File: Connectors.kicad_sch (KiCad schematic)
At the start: 4 parts, among them J1 Conn_01x09_Pin, J2 Conn_02x03_Odd_Even

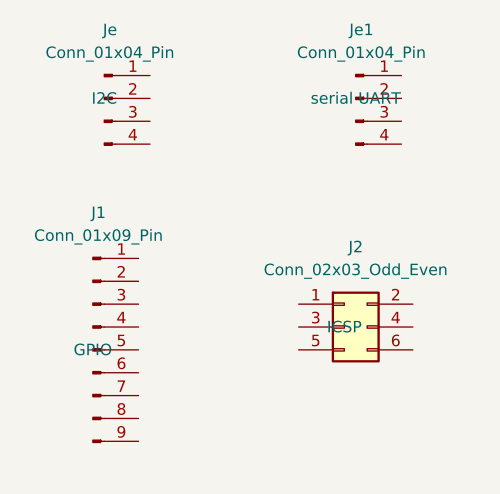
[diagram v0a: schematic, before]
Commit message: Changed location of symbols (arrange).
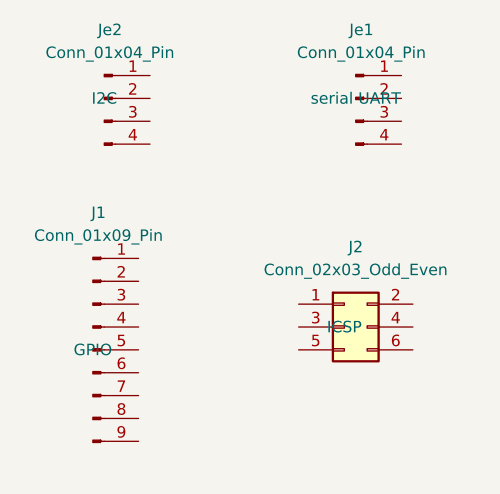
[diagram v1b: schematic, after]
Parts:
- renumbered Je to Je2
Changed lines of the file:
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@@
 		(dnp no)
 		(fields_autoplaced yes)
-		(property "Reference" "Je"
+		(property "Reference" "Je2"
 			(at 121.285 81.28 0)
 			(effects
@@
 			(project ""
 				(path "/b34ba724-37f1-4069-92d1-dfc9c20970e0/121f44e2-27fc-4ef2-96b3-bc3990488b1d"
-					(reference "Je")
+					(reference "Je2")
 					(unit 1)
 				)

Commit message: completed symbol-footprint assiciations
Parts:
- J1: footprint (none) -> Connector_PinHeader_2.54mm:PinHeader_1x09_P2.54mm_Vertical
- J2: footprint (none) -> Connector_PinHeader_2.54mm:PinHeader_2x03_P2.54mm_Vertical
- Je1, Je2: footprint (none) -> Connector_PinHeader_2.54mm:PinHeader_1x04_P2.54mm_Vertical
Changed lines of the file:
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@@
 			)
 		)
-		(property "Footprint" ""
+		(property "Footprint" "Connector_PinHeader_2.54mm:PinHeader_1x04_P2.54mm_Vertical"
 			(at 148.59 88.9 0)
 			(effects
@@
 			)
 		)
-		(property "Footprint" ""
+		(property "Footprint" "Connector_PinHeader_2.54mm:PinHeader_1x09_P2.54mm_Vertical"
 			(at 119.38 116.84 0)
 			(effects
@@
 			)
 		)
-		(property "Footprint" ""
+		(property "Footprint" "Connector_PinHeader_2.54mm:PinHeader_2x03_P2.54mm_Vertical"
 			(at 147.32 114.3 0)
 			(effects
@@
 			)
 		)
-		(property "Footprint" ""
+		(property "Footprint" "Connector_PinHeader_2.54mm:PinHeader_1x04_P2.54mm_Vertical"
 			(at 120.65 88.9 0)
 			(effects

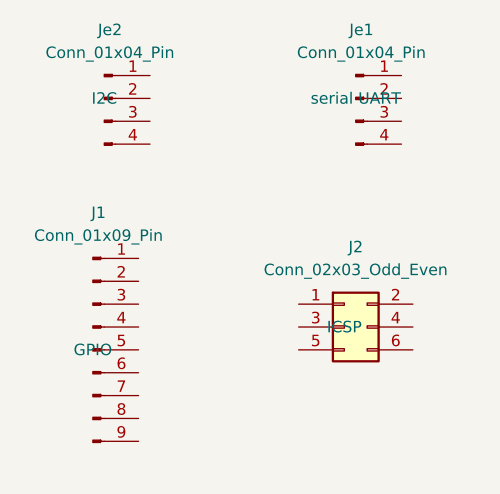
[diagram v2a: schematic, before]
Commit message: completed wiring in the second sheet.
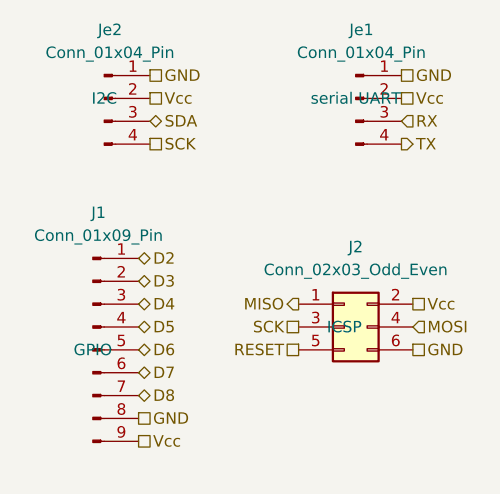
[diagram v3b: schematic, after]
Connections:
- net GND: now reaches Je1.1 (Pin_1)
- net GND: now also J1.8 (Pin_8), J2.6 (Pin_6), Je2.1 (Pin_1)
- net Vcc: now reaches Je1.2 (Pin_2)
- net Vcc: now also J1.9 (Pin_9), J2.2 (Pin_2), Je2.2 (Pin_2)
- net RX: now reaches Je1.3 (Pin_3)
- net TX: now reaches Je1.4 (Pin_4)
- net D2: now reaches J1.1 (Pin_1)
- net D3: now reaches J1.2 (Pin_2)
- net D4: now reaches J1.3 (Pin_3)
- net D5: now reaches J1.4 (Pin_4)
- net D6: now reaches J1.5 (Pin_5)
- net D7: now reaches J1.6 (Pin_6)
- net D8: now reaches J1.7 (Pin_7)
- net MISO: now reaches J2.1 (Pin_1)
- net SCK: now reaches J2.3 (Pin_3)
- net SCK: now also Je2.4 (Pin_4)
- net MOSI: now reaches J2.4 (Pin_4)
- net RESET: now reaches J2.5 (Pin_5)
- net SDA: now reaches Je2.3 (Pin_3)
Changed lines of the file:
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@@
 	(generator_version "9.0")
 	(paper "A4")
+	(hierarchical_label "D2"
+		(shape bidirectional)
+		(at 124.46 106.68 0)
+		(effects
+			(font
+				(size 1.27 1.27)
+			)
+			(justify left)
+		)
+	)
+	(hierarchical_label "RX"
+		(shape input)
+		(at 153.67 91.44 0)
+		(effects
+			(font
+				(size 1.27 1.27)
+			)
+			(justify left)
+		)
+	)
+	(hierarchical_label "MISO"
+		(shape output)
+		(at 142.24 111.76 180)
+		(effects
+			(font
+				(size 1.27 1.27)
+			)
+			(justify right)
+		)
+	)
+	(hierarchical_label "GND"
+		(shape passive)
+		(at 154.94 116.84 0)
+		(effects
+			(font
+				(size 1.27 1.27)
+			)
+			(justify left)
+		)
+	)
+	(hierarchical_label "Vcc"
+		(shape passive)
+		(at 153.67 88.9 0)
+		(effects
+			(font
+				(size 1.27 1.27)
+			)
+			(justify left)
+		)
+	)
+	(hierarchical_label "TX"
+		(shape output)
+		(at 153.67 93.98 0)
+		(effects
+			(font
+				(size 1.27 1.27)
+			)
+			(justify left)
+		)
+	)
+	(hierarchical_label "Vcc"
+		(shape passive)
+		(at 125.73 88.9 0)
+		(effects
+			(font
+				(size 1.27 1.27)
+			)
+			(justify left)
+		)
+	)
+	(hierarchical_label "Vcc"
+		(shape passive)
+		(at 154.94 111.76 0)
+		(effects
+			(font
+				(size 1.27 1.27)
+			)
+			(justify left)
+		)
+	)
+	(hierarchical_label "SCK"
+		(shape passive)
+		(at 142.24 114.3 180)
+		(effects
+			(font
+				(size 1.27 1.27)
+			)
+			(justify right)
+		)
+	)
+	(hierarchical_label "MOSI"
+		(shape input)
+		(at 154.94 114.3 0)
+		(effects
+			(font
+				(size 1.27 1.27)
+			)
+			(justify left)
+		)
+	)
+	(hierarchical_label "SDA"
+		(shape bidirectional)
+		(at 125.73 91.44 0)
+		(effects
+			(font
+				(size 1.27 1.27)
+			)
+			(justify left)
+		)
+	)
+	(hierarchical_label "D7"
+		(shape bidirectional)
+		(at 124.46 119.38 0)
+		(effects
+			(font
+				(size 1.27 1.27)
+			)
+			(justify left)
+		)
+	)
+	(hierarchical_label "D5"
+		(shape bidirectional)
+		(at 124.46 114.3 0)
+		(effects
+			(font
+				(size 1.27 1.27)
+			)
+			(justify left)
+		)
+	)
+	(hierarchical_label "GND"
+		(shape passive)
+		(at 124.46 124.46 0)
+		(effects
+			(font
+				(size 1.27 1.27)
+			)
+			(justify left)
+		)
+	)
+	(hierarchical_label "D3"
+		(shape bidirectional)
+		(at 124.46 109.22 0)
+		(effects
+			(font
+				(size 1.27 1.27)
+			)
+			(justify left)
+		)
+	)
+	(hierarchical_label "RESET"
+		(shape passive)
+		(at 142.24 116.84 180)
+		(effects
+			(font
+				(size 1.27 1.27)
+			)
+			(justify right)
+		)
+	)
+	(hierarchical_label "GND"
+		(shape passive)
+		(at 153.67 86.36 0)
+		(effects
+			(font
+				(size 1.27 1.27)
+			)
+			(justify left)
+		)
+	)
+	(hierarchical_label "Vcc"
+		(shape passive)
+		(at 124.46 127 0)
+		(effects
+			(font
+				(size 1.27 1.27)
+			)
+			(justify left)
+		)
+	)
+	(hierarchical_label "GND"
+		(shape passive)
+		(at 125.73 86.36 0)
+		(effects
+			(font
+				(size 1.27 1.27)
+			)
+			(justify left)
+		)
+	)
+	(hierarchical_label "D6"
+		(shape bidirectional)
+		(at 124.46 116.84 0)
+		(effects
+			(font
+				(size 1.27 1.27)
+			)
+			(justify left)
+		)
+	)
+	(hierarchical_label "SCK"
+		(shape passive)
+		(at 125.73 93.98 0)
+		(effects
+			(font
+				(size 1.27 1.27)
+			)
+			(justify left)
+		)
+	)
+	(hierarchical_label "D8"
+		(shape bidirectional)
+		(at 124.46 121.92 0)
+		(effects
+			(font
+				(size 1.27 1.27)
+			)
+			(justify left)
+		)
+	)
+	(hierarchical_label "D4"
+		(shape bidirectional)
+		(at 124.46 111.76 0)
+		(effects
+			(font
+				(size 1.27 1.27)
+			)
+			(justify left)
+		)
+	)
 	(symbol
 		(lib_id "Connector:Conn_01x04_Pin")

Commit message: finshing silkscreen.
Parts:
- renumbered Je2 to J1, J1 to J2, Je1 to J3, J2 to J4
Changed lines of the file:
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@@
 		(on_board yes)
 		(dnp no)
-		(fields_autoplaced yes)
-		(property "Reference" "Je1"
+		(property "Reference" "J3"
 			(at 149.225 81.28 0)
 			(effects
@@
 		)
 		(property "Purpose" "serial UART"
-			(at 148.59 88.9 0)
+			(at 152.4 96.52 0)
 			(effects
 				(font
@@
 			(project "MCU Datalogger"
 				(path "/b34ba724-37f1-4069-92d1-dfc9c20970e0/121f44e2-27fc-4ef2-96b3-bc3990488b1d"
-					(reference "Je1")
+					(reference "J3")
 					(unit 1)
 				)
@@
 		(on_board yes)
 		(dnp no)
-		(fields_autoplaced yes)
-		(property "Reference" "J1"
+		(property "Reference" "J2"
 			(at 120.015 101.6 0)
 			(effects
@@
 		)
 		(property "Purpose" "GPIO"
-			(at 119.38 116.84 0)
+			(at 123.19 129.54 0)
 			(effects
 				(font
@@
 			(project ""
 				(path "/b34ba724-37f1-4069-92d1-dfc9c20970e0/121f44e2-27fc-4ef2-96b3-bc3990488b1d"
-					(reference "J1")
+					(reference "J2")
 					(unit 1)
 				)
@@
 		(on_board yes)
 		(dnp no)
-		(fields_autoplaced yes)
-		(property "Reference" "J2"
+		(property "Reference" "J4"
 			(at 148.59 105.41 0)
 			(effects
@@
 		)
 		(property "Purpose" "ICSP"
-			(at 147.32 114.3 0)
+			(at 148.59 119.38 0)
 			(effects
 				(font
@@
 			(project ""
 				(path "/b34ba724-37f1-4069-92d1-dfc9c20970e0/121f44e2-27fc-4ef2-96b3-bc3990488b1d"
-					(reference "J2")
+					(reference "J4")
 					(unit 1)
 				)
@@
 		(on_board yes)
 		(dnp no)
-		(fields_autoplaced yes)
-		(property "Reference" "Je2"
+		(property "Reference" "J1"
 			(at 121.285 81.28 0)
 			(effects
@@
 		)
 		(property "Purpose" "I2C"
-			(at 120.65 88.9 0)
+			(at 124.46 96.52 0)
 			(effects
 				(font
@@
 			(project ""
 				(path "/b34ba724-37f1-4069-92d1-dfc9c20970e0/121f44e2-27fc-4ef2-96b3-bc3990488b1d"
-					(reference "Je2")
+					(reference "J1")
 					(unit 1)
 				)

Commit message: fix the bugs in the schematic.
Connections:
- net SCK: no longer J1.4 (Pin_4)
- new net SCL: J1.4 (Pin_4)
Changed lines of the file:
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@@
 		)
 	)
-	(hierarchical_label "SCK"
+	(hierarchical_label "SCL"
 		(shape passive)
 		(at 125.73 93.98 0)
